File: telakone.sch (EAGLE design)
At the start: 145 parts, among them X11 MPT0.5/8-2.54, X2 MPT0.5/8-2.54, X3 MPT0.5/8-2.54, X4 PIIKKIRIMA-2, X5 PIIKKIRIMA-5, X7 U.FL-R-SMT-1, X8 MPT0.5/8-2.54, X9 629105136821

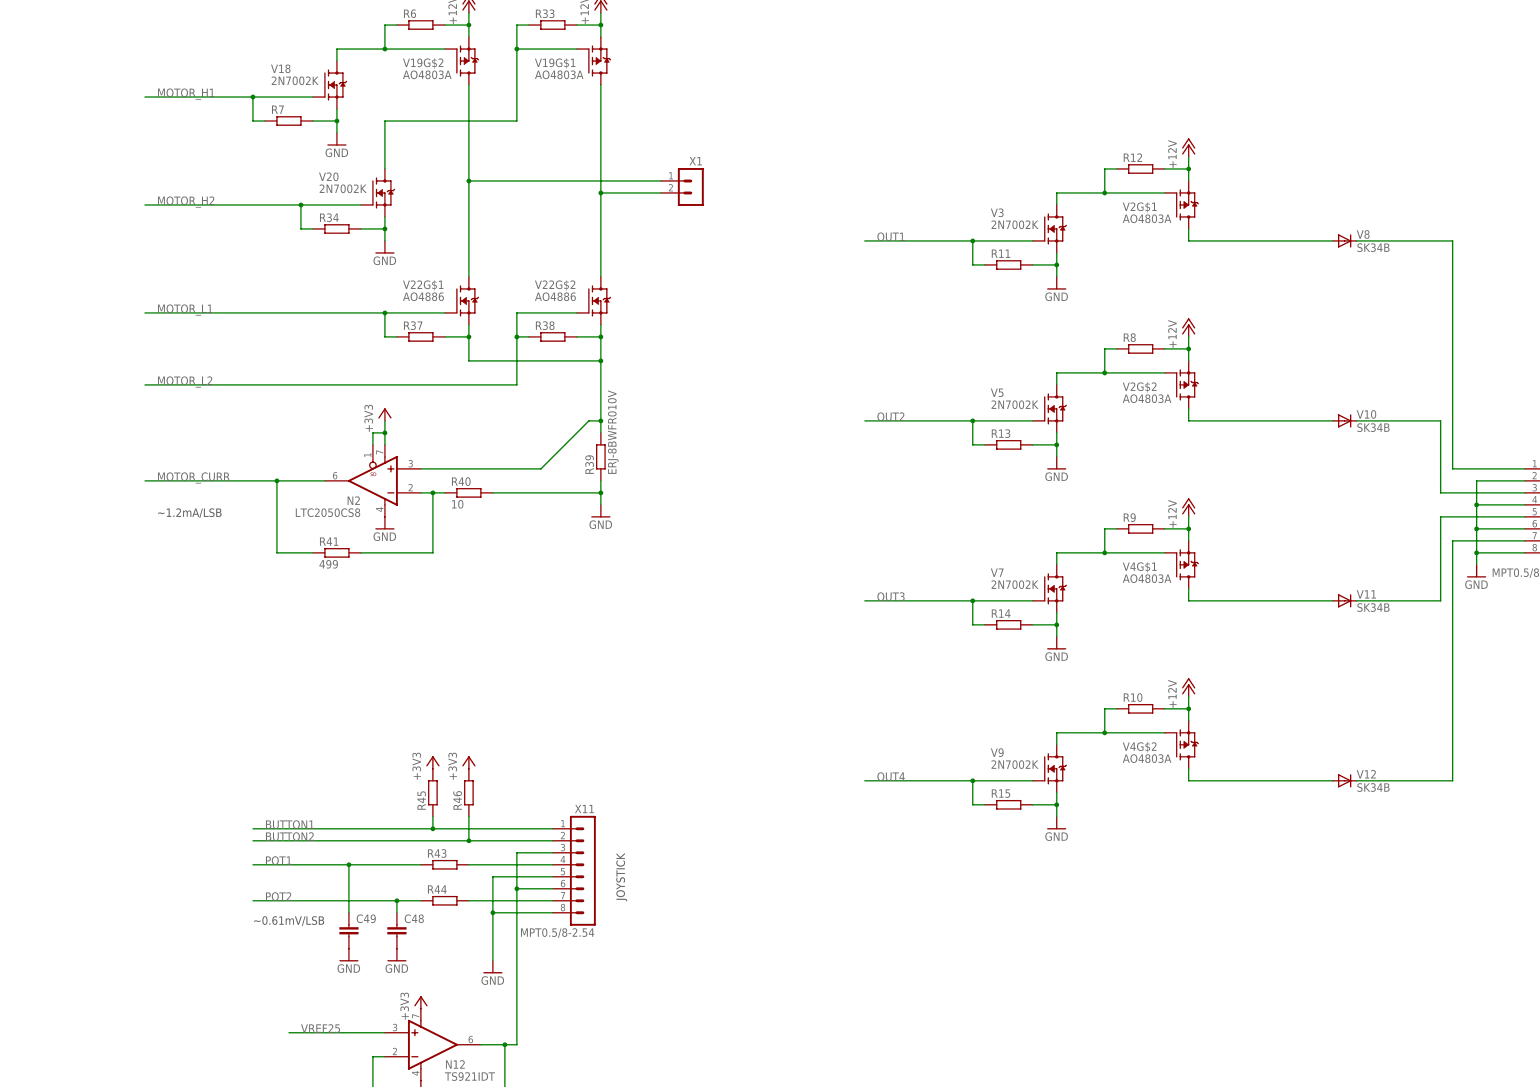
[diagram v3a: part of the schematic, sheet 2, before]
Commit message: add some protection
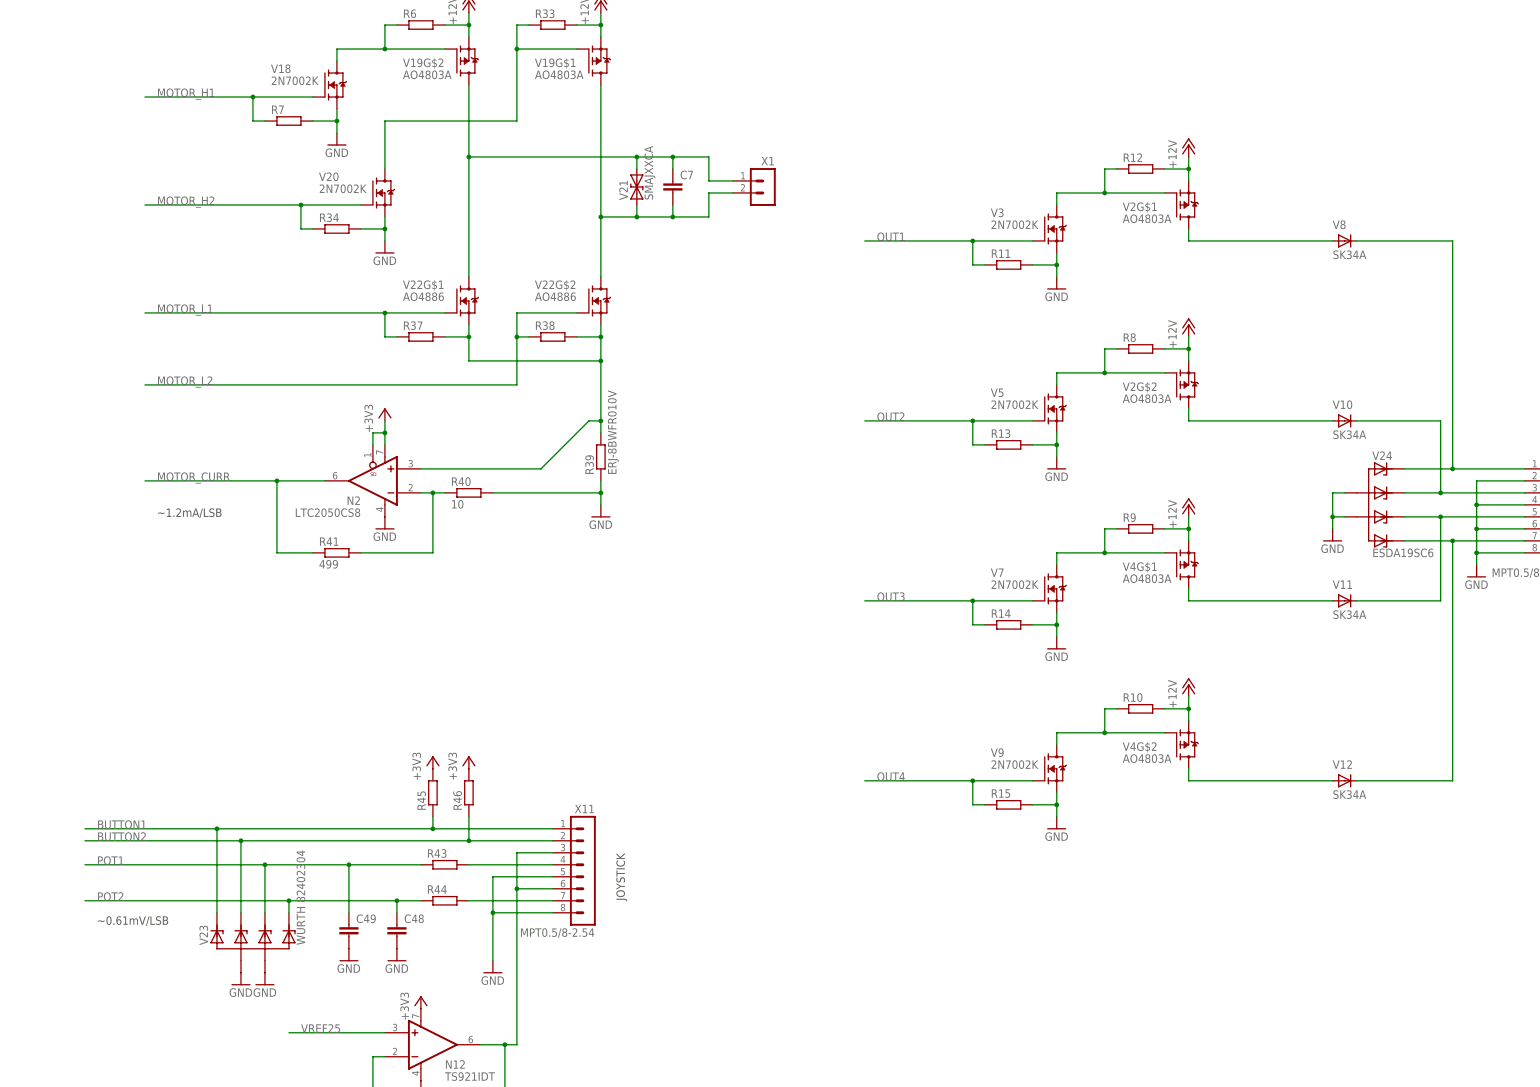
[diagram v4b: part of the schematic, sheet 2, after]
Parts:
- added C7: (no value), omat_ic_2:CAP0603
- added F1: KEYSTONE-3549-2, omat_ic_2:KEYSTONE-3549-2
- added V21: SMAJXXCA, omat_ic_2:SMAJXXCA
- added V23: WURTH 82402304, omat_ic_2:ESDAXXSC6
- added V24: ESDA19SC6, omat_ic_2:ESDAXXSC6
- added V25: ESDAXXSC6, omat_ic_2:ESDAXXSC6
- V10, V11, V12, V13, V8: value SK34B -> SK34A; device diode:DIODE-SMB -> omat_ic_2:SK34A
- V14: value 1SMA5.0AT -> ESDAXXSC6; device EKE:1SMA5913BT3 -> omat_ic_2:ESDAXXSC6
- V15, V17: value 1SMA5.0AT -> SMAJ5.0A; device EKE:1SMA5913BT3 -> omat_ic_2:SMAJXXA
- V16: value 1SMA5.0AT -> SMAJXXA; device EKE:1SMA5913BT3 -> omat_ic_2:SMAJXXA
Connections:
- new net N$8: F1.2, X6.1
- net +12V: now also F1.1, V16.C; no longer X6.1
- net AIN_1: now also V14.C3; no longer V14.C
- net AIN_2: now also V25.C3; no longer V16.C
- net BRAKE_OD_1: now also V14.C1
- net BRAKE_OD_2: now also V25.C1
- net BUTTON1: now also V23.C
- net BUTTON2: now also V23.C1
- net GND: now also V16.A, V23.A, V23.A1, V24.A, V24.A1
- net N$17: now also V24.C3
- net N$19: now also V24.C2
- net N$20: now also V24.C1
- net N$21: now also V24.C
- net NERT4: now also C7.1, V21.2
- net NERT5: now also C7.2, V21.1
- net POT1: now also V23.C2
- net POT2: now also V23.C3
- net REVERSE_OD_1: now also V14.C
- net REVERSE_OD_2: now also V25.C
- net THROTTLE_BUFFERED_1: now also V14.C2
- net THROTTLE_BUFFERED_2: now also V25.C2
- net V-1: now also V14.A1
- net V-2: now also V25.A, V25.A1; no longer V16.A
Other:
- moved on the sheet: X1, X6

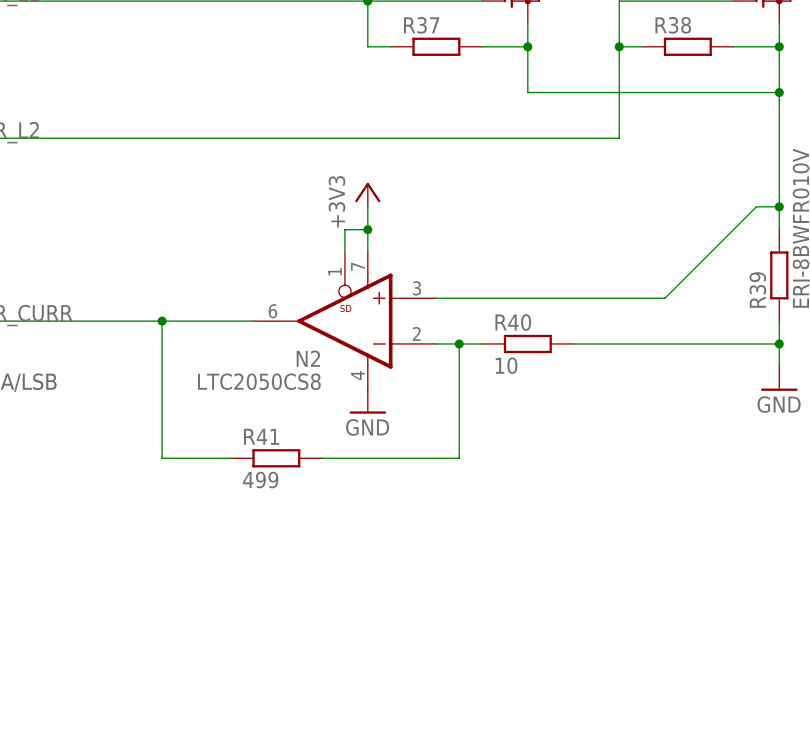
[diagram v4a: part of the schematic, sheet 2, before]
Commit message: Schematics tuning
Series resistors to SWDIO/SWCLK
Pulldown to DAC outputs (HighZ after powerup)
Some missing values added
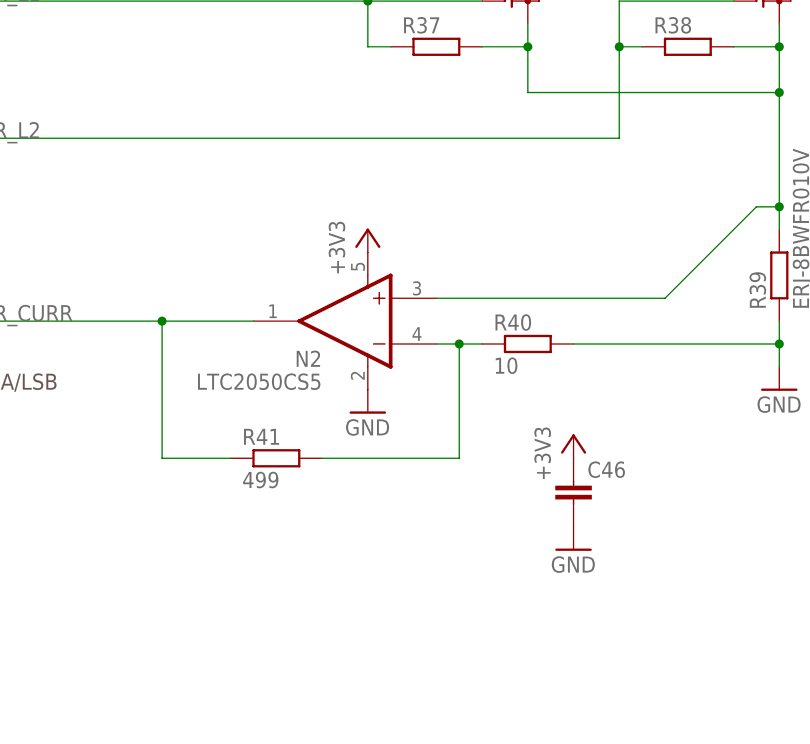
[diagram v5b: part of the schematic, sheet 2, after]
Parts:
- added C46: (no value), omat_ic_2:CAP0603
- added R42, R47: (no value), omat_ic_2:RES0603
- added R48, R49: 100k, omat_ic_2:RES0603
- C10, C13, C14, C15, C16, C17, C18, C19, C20, C21, C22, C26, C27, C31, C32, C33, C34, C35, C36, C40, C41, C42, C43, C44: value (none) -> 100n
- C11, C12, C28, C29, C30, C39, C6: value (none) -> 2u2
- N2: value LTC2050CS8 -> LTC2050CS5; device omat_ic_2:LTC2050CS8 -> omat_ic_2:LTC2050CS5
- R17, R32, R5: value (none) -> 1k
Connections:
- new net N$16: D1G$1.PA14/TCK/SWCLK, R47.2
- new net N$22: D1G$1.PA13/TMS/SWDIO, R42.2
- net +3V3: now also C46.1; no longer N2.SD
- net GND: now also C46.2
- net SWCLK: now also R47.1; no longer D1G$1.PA14/TCK/SWCLK
- net SWDIO: now also R42.1; no longer D1G$1.PA13/TMS/SWDIO
- net THROTTLE_1: now also R49.2
- net THROTTLE_2: now also R48.2
- net V-1: now also R49.1
- net V-2: now also R48.1

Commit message: speed sensor inputs
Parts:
- removed C48, C49: (no value), omat_ic_2:CAP0603
- removed V23: WURTH 82402304, omat_ic_2:ESDAXXSC6
- added C50, C51: (no value), omat_ic_2:CAP0603
- added N13: TS921IDT, omat_ic_2:TS921IDT
- added R50, R51: (no value), omat_ic_2:RES0603
- added R52, R53: 2k00, omat_ic_2:RES0603
- added R54, R55: 30k1, omat_ic_2:RES0603
- added R56, R57: 5k90, omat_ic_2:RES0603
- added V26: WURTH 82402304, omat_ic_2:ESDAXXSC6
- added X10: MPT0.5/8-2.54, omat_ic_2:MPT0.5/8-2.54
- N12: value TS921IDT -> AZV3002S; device omat_ic_2:TS921IDT -> omat_ic_2:AZV3002S
- R28, R29, R46: value (none) -> 2k00
- R43, R44: value (none) -> 1k
- R45: value (none) -> 499
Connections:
- new net N$25: R50.2, X10.4
- new net N$43: R51.2, X10.7
- new net SPEED1: D1G$2.PD12, N12G$1.OUT
- new net SPEED2: D1G$2.PD13, N12G$2.OUT
- new net SPEED_SENSOR_1: R43.1, R54.2, X11.2
- new net SPEED_SENSOR_2: R44.1, R55.2, X11.5
- new net VREF25BUF: N13.-IN, N13.OUT, R46.2, X10.3, X10.6
- net +12V: now also R43.2, R44.2, X11.1, X11.4
- net +3V3: now also N12G$1.V+, N13.V+, R52.2, R53.2; no longer N12.V+, R45.2, R46.2
- net BUTTON1: now also R52.1, V26.C, X10.1; no longer R45.1, V23.C, X11.1
- net BUTTON2: now also R53.1, V26.C1, X10.2; no longer R46.1, V23.C1, X11.2
- net GND: now also C50.2, C51.2, N12G$1.V-, N13.V-, R45.1, R56.1, R57.1, V26.A, V26.A1, X10.5, X10.8, X11.3, X11.6; no longer C48.2, C49.2, N12.V-, V23.A, V23.A1, X11.5
- net N$12: now also N12G$2.+IN, R55.1, R57.2; no longer R43.2, X11.4
- net N$14: now also N12G$1.-IN, N12G$2.-IN, R45.2, R46.1; no longer R44.2, X11.7
- net N$5: now also N12G$1.+IN, R54.1, R56.2; no longer N12.-IN, N12.OUT, X11.3, X11.6
- net POT1: now also C51.1, R50.1, V26.C2; no longer C49.1, R43.1, V23.C2
- net POT2: now also C50.1, R51.1, V26.C3; no longer C48.1, R44.1, V23.C3
- net VREF25: now also N13.+IN; no longer N12.+IN
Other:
- note added: "SPEED SENSORS"
- note added: "THRESHOLD ~6 V MAX INPUT 20V"
- note added: "TIM4_CH1"
- note added: "TIM4_CH2"
